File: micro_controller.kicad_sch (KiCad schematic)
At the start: 14 parts, among them J2 Conn_01x06_Male, Q7 DMN62D0U-7, U3 MCP2221A, U6 ESP32

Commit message: WIP
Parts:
- added JP3: Jumper_2_Open, Connector_PinHeader_2.54mm:PinHeader_1x02_P2.54mm_Vertical, symbol Jumper:Jumper_2_Open
- added R28: R, Resistor_SMD:R_0805_2012Metric, symbol Device:R
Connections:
- net GND: now also R7.2, R8.2, R28.2; no longer D10.1, D4.1
- net GPIO_{DATA}: now also U6.10 (IO25); no longer U6.28 (IO17)
- net GPIO_{RCLK}: now also U6.8 (IO32); no longer U6.30 (IO18)
- net GPIO_{SCLK}: now also U6.9 (IO33); no longer U6.29 (IO5)
- net SPI.CLK: now also U6.29 (IO5); no longer U6.10 (IO25)
- net SPI.MISO: now also U6.27 (IO16); no longer U6.8 (IO32)
- net SPI.MOSI: now also U6.28 (IO17); no longer U6.9 (IO33)
- net bootmode_select: now also JP3.1 (A)
- net mcu_indicator: now also D10.2, U6.33 (IO21); no longer R8.1
- net usb_indicator: now also D4.2; no longer R7.1
- net ~{GPIO_{OE}}: now also U6.12 (IO27); no longer U6.26 (IO4)
- net ~{GPIO_{RS}}: now also U6.11 (IO26); no longer U6.27 (IO16)
- net ~{INT_{CAN}}: now also U6.30 (IO18); no longer U6.12 (IO27)
- net ~{SPI.CS_{CAN}}: now also U6.26 (IO4); no longer U6.11 (IO26)
- new net: D4.1, R7.1
- new net: JP3.2 (B), R28.1
- new net: D10.1, R8.1
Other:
- note added: "Use to manually put ESP into boot mode"
- moved on the sheet: D10, D4, R7, R8

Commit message: WIP
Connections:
- net GPIO_{DATA}: now also U6.9 (IO33); no longer U6.10 (IO25)
- net GPIO_{RCLK}: now also U6.11 (IO26); no longer U6.8 (IO32)
- net GPIO_{SCLK}: now also U6.8 (IO32); no longer U6.9 (IO33)
- net ~{GPIO_{RS}}: now also U6.10 (IO25); no longer U6.11 (IO26)
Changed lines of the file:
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@@
     (effects (font (size 1.27 1.27)) (justify right))
   )
-  (hierarchical_label "GPIO_{RCLK}" (shape output) (at 148.59 96.52 180)
+  (hierarchical_label "GPIO_{SCLK}" (shape output) (at 148.59 96.52 180)
     (effects (font (size 1.27 1.27)) (justify right))
   )
-  (hierarchical_label "GPIO_{SCLK}" (shape output) (at 148.59 99.06 180)
+  (hierarchical_label "GPIO_{DATA}" (shape output) (at 148.59 99.06 180)
     (effects (font (size 1.27 1.27)) (justify right))
   )
-  (hierarchical_label "GPIO_{DATA}" (shape output) (at 148.59 101.6 180)
+  (hierarchical_label "~{GPIO_{RS}}" (shape output) (at 148.59 101.6 180)
     (effects (font (size 1.27 1.27)) (justify right))
   )
-  (hierarchical_label "~{GPIO_{RS}}" (shape output) (at 148.59 104.14 180)
+  (hierarchical_label "GPIO_{RCLK}" (shape output) (at 148.59 104.14 180)
     (effects (font (size 1.27 1.27)) (justify right))
   )

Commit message: WIP
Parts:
- removed J2: Conn_01x06_Male, Connector_PinHeader_2.54mm:PinHeader_2x03_P2.54mm_Vertical, symbol Connector:Conn_01x06_Male
- added J2: Conn_01x12_Male, Connector_PinHeader_2.54mm:PinHeader_2x06_P2.54mm_Vertical, symbol Connector:Conn_01x12_Male
- added R32, R33, R34: R, Resistor_SMD:R_0805_2012Metric, symbol Device:R
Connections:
- net GND: now also J2.6 (Pin_6), J2.9 (Pin_9)
- net SCL: now also J2.5 (Pin_5)
- net SDA: now also J2.3 (Pin_3)
- net bootmode_select: now also R34.1
- net esp_reset: now also U3.8 (GP3), R33.1
- net esp_rx: now also J2.8 (Pin_8)
- net esp_tx: now also R32.1
- net ~silent_boot: now also J2.7 (Pin_7)
- new net: J2.11 (Pin_11), R33.2
- new net: J2.10 (Pin_10), R32.2
- new net: J2.12 (Pin_12), R34.2
- new net +5V: J2.2 (Pin_2), J2.4 (Pin_4)
- no-connect marks 2 -> 3
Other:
- note added: "This header provides access to the ESP's UART, strapping pins, and I2C bus. It is designed to match the pinout of pins 1-12 of the Raspberry Pi such that a cable can connect them directly to supply data and power."
- note removed: "Debug Header"
- moved on the sheet: JP10, JP9, U3, U6

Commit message: geographical reannotate
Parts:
- renumbered C5 to C17, C6 to C2, C8 to C23, D10 to D4, D4 to D7, J2 to J1, JP3 to JP1, JP9 to JP2, JP10 to JP3, Q7 to Q1, R6 to R1, R8 to R16, R28 to R17, R34 to R18, R33 to R19, R32 to R21, R7 to R23, U6 to U1
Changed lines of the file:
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@@
   (symbol (lib_id "Jumper:SolderJumper_2_Open") (at 48.26 77.47 180) (unit 1)
     (in_bom yes) (on_board yes)
-    (property "Reference" "JP10" (id 0) (at 44.45 76.2 0)
+    (property "Reference" "JP3" (id 0) (at 44.45 76.2 0)
       (effects (font (size 1.27 1.27)) (justify left))
     )
@@
   (symbol (lib_id "Jumper:SolderJumper_2_Open") (at 48.26 80.01 180) (unit 1)
     (in_bom yes) (on_board yes)
-    (property "Reference" "JP9" (id 0) (at 43.18 78.74 0)
+    (property "Reference" "JP2" (id 0) (at 43.18 78.74 0)
       (effects (font (size 1.27 1.27)) (justify left))
     )
@@
   (symbol (lib_id "Device:R") (at 48.26 161.29 0) (unit 1)
     (in_bom yes) (on_board yes) (fields_autoplaced)
-    (property "Reference" "R6" (id 0) (at 50.8 160.0199 0)
+    (property "Reference" "R1" (id 0) (at 50.8 160.0199 0)
       (effects (font (size 1.27 1.27)) (justify left))
     )
@@
   (symbol (lib_id "Device:R") (at 76.2 181.61 0) (unit 1)
     (in_bom yes) (on_board yes) (fields_autoplaced)
-    (property "Reference" "R7" (id 0) (at 78.74 180.3399 0)
+    (property "Reference" "R23" (id 0) (at 78.74 180.3399 0)
       (effects (font (size 1.27 1.27)) (justify left))
     )
@@
   (symbol (lib_id "Device:R") (at 86.36 181.61 0) (unit 1)
     (in_bom yes) (on_board yes) (fields_autoplaced)
-    (property "Reference" "R8" (id 0) (at 88.9 180.3399 0)
+    (property "Reference" "R16" (id 0) (at 88.9 180.3399 0)
       (effects (font (size 1.27 1.27)) (justify left))
     )
@@
   (symbol (lib_id "Device:R") (at 147.32 180.34 0) (unit 1)
     (in_bom yes) (on_board yes) (fields_autoplaced)
-    (property "Reference" "R28" (id 0) (at 149.86 179.0699 0)
+    (property "Reference" "R17" (id 0) (at 149.86 179.0699 0)
       (effects (font (size 1.27 1.27)) (justify left))
     )
@@
   (symbol (lib_id "Device:R") (at 250.19 48.26 90) (unit 1)
     (in_bom yes) (on_board yes)
-    (property "Reference" "R32" (id 0) (at 255.27 46.99 90))
+    (property "Reference" "R21" (id 0) (at 255.27 46.99 90))
     (property "Value" "R" (id 1) (at 250.19 48.26 90))
     (property "Footprint" "Resistor_SMD:R_0805_2012Metric" (id 2) (at 250.19 50.038 90)
@@
   (symbol (lib_id "Device:R") (at 250.19 50.8 90) (unit 1)
     (in_bom yes) (on_board yes)
-    (property "Reference" "R33" (id 0) (at 255.27 49.53 90))
+    (property "Reference" "R19" (id 0) (at 255.27 49.53 90))
     (property "Value" "R" (id 1) (at 250.19 50.8 90))
     (property "Footprint" "Resistor_SMD:R_0805_2012Metric" (id 2) (at 250.19 52.578 90)
@@
   (symbol (lib_id "Device:R") (at 250.19 53.34 90) (unit 1)
     (in_bom yes) (on_board yes)
-    (property "Reference" "R34" (id 0) (at 255.27 52.07 90))
+    (property "Reference" "R18" (id 0) (at 255.27 52.07 90))
     (property "Value" "R" (id 1) (at 250.19 53.34 90))
     (property "Footprint" "Resistor_SMD:R_0805_2012Metric" (id 2) (at 250.19 55.118 90)
@@
   (symbol (lib_id "Jumper:Jumper_2_Open") (at 147.32 171.45 270) (unit 1)
     (in_bom yes) (on_board yes)
-    (property "Reference" "JP3" (id 0) (at 149.86 170.1799 90)
+    (property "Reference" "JP1" (id 0) (at 149.86 170.1799 90)
       (effects (font (size 1.27 1.27)) (justify left))
     )
@@
   (symbol (lib_id "ecafe-racer:LED_Green") (at 76.2 173.99 90) (unit 1)
     (in_bom yes) (on_board yes) (fields_autoplaced)
-    (property "Reference" "D4" (id 0) (at 80.01 172.9104 90)
+    (property "Reference" "D7" (id 0) (at 80.01 172.9104 90)
       (effects (font (size 1.27 1.27)) (justify right))
     )
@@
   (symbol (lib_id "ecafe-racer:LED_Green") (at 86.36 173.99 90) (unit 1)
     (in_bom yes) (on_board yes) (fields_autoplaced)
-    (property "Reference" "D10" (id 0) (at 90.17 172.9104 90)
+    (property "Reference" "D4" (id 0) (at 90.17 172.9104 90)
       (effects (font (size 1.27 1.27)) (justify right))
     )
@@
   (symbol (lib_id "Device:C") (at 48.26 175.26 0) (unit 1)
     (in_bom yes) (on_board yes) (fields_autoplaced)
-    (property "Reference" "C5" (id 0) (at 52.07 173.9899 0)
+    (property "Reference" "C17" (id 0) (at 52.07 173.9899 0)
       (effects (font (size 1.27 1.27)) (justify left))
     )
@@
   (symbol (lib_id "Device:C") (at 204.47 152.4 0) (unit 1)
     (in_bom yes) (on_board yes) (fields_autoplaced)
-    (property "Reference" "C6" (id 0) (at 208.28 151.1299 0)
+    (property "Reference" "C2" (id 0) (at 208.28 151.1299 0)
       (effects (font (size 1.27 1.27)) (justify left))
     )
@@
   (symbol (lib_id "Device:C") (at 217.17 152.4 0) (unit 1)
     (in_bom yes) (on_board yes) (fields_autoplaced)
-    (property "Reference" "C8" (id 0) (at 220.98 151.1299 0)
+    (property "Reference" "C23" (id 0) (at 220.98 151.1299 0)
       (effects (font (size 1.27 1.27)) (justify left))
     )
@@
   (symbol (lib_id "ecafe-racer:DMN62D0U-7") (at 39.37 175.26 0) (unit 1)
     (in_bom yes) (on_board yes)
-    (property "Reference" "Q7" (id 0) (at 31.75 170.1799 0)
+    (property "Reference" "Q1" (id 0) (at 31.75 170.1799 0)
       (effects (font (size 1.27 1.27)) (justify left))
     )
@@
   (symbol (lib_id "Connector:Conn_01x12_Male") (at 265.43 38.1 0) (mirror y) (unit 1)
     (in_bom yes) (on_board yes)
-    (property "Reference" "J2" (id 0) (at 267.97 38.0999 0)
+    (property "Reference" "J1" (id 0) (at 267.97 38.0999 0)
       (effects (font (size 1.27 1.27)) (justify right))
     )
@@
   (symbol (lib_id "ecafe-racer:ESP32") (at 156.21 74.93 0) (unit 1)
     (in_bom yes) (on_board yes) (fields_autoplaced)
-    (property "Reference" "U6" (id 0) (at 155.575 46.99 0))
+    (property "Reference" "U1" (id 0) (at 155.575 46.99 0))
     (property "Value" "ESP32" (id 1) (at 155.575 49.53 0))
     (property "Footprint" "ecafe-racer:MODULE_ESP32-WROOM-32" (id 2) (at 149.606 50.038 0)

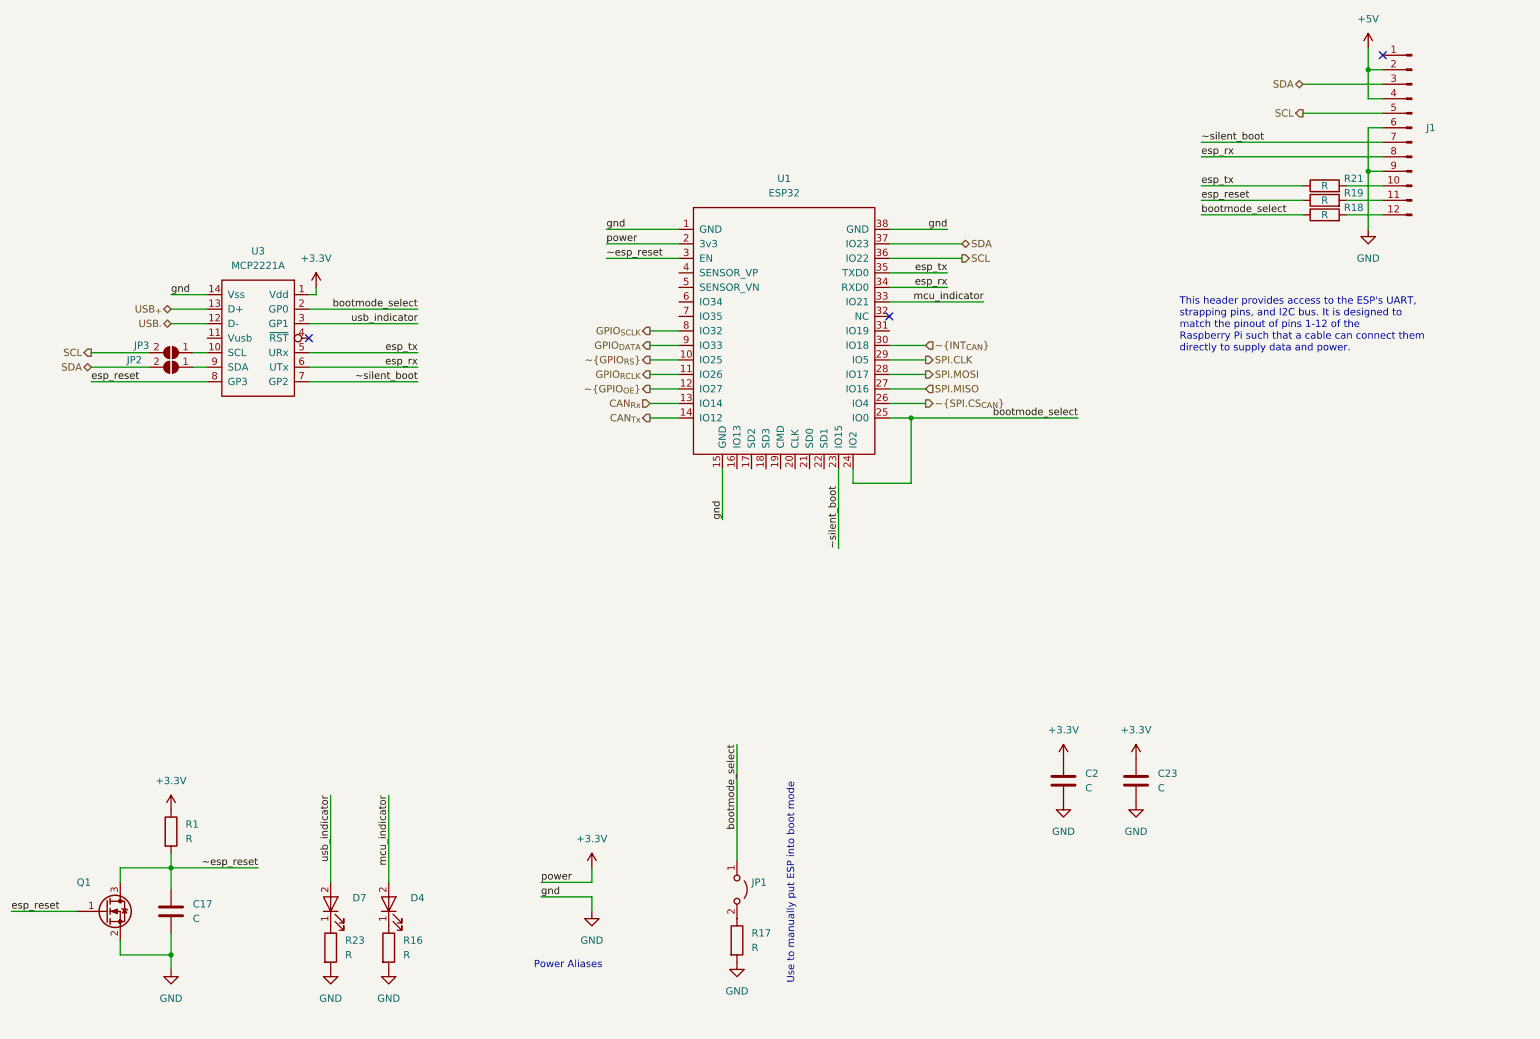
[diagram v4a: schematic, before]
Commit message: cleaned up schematic
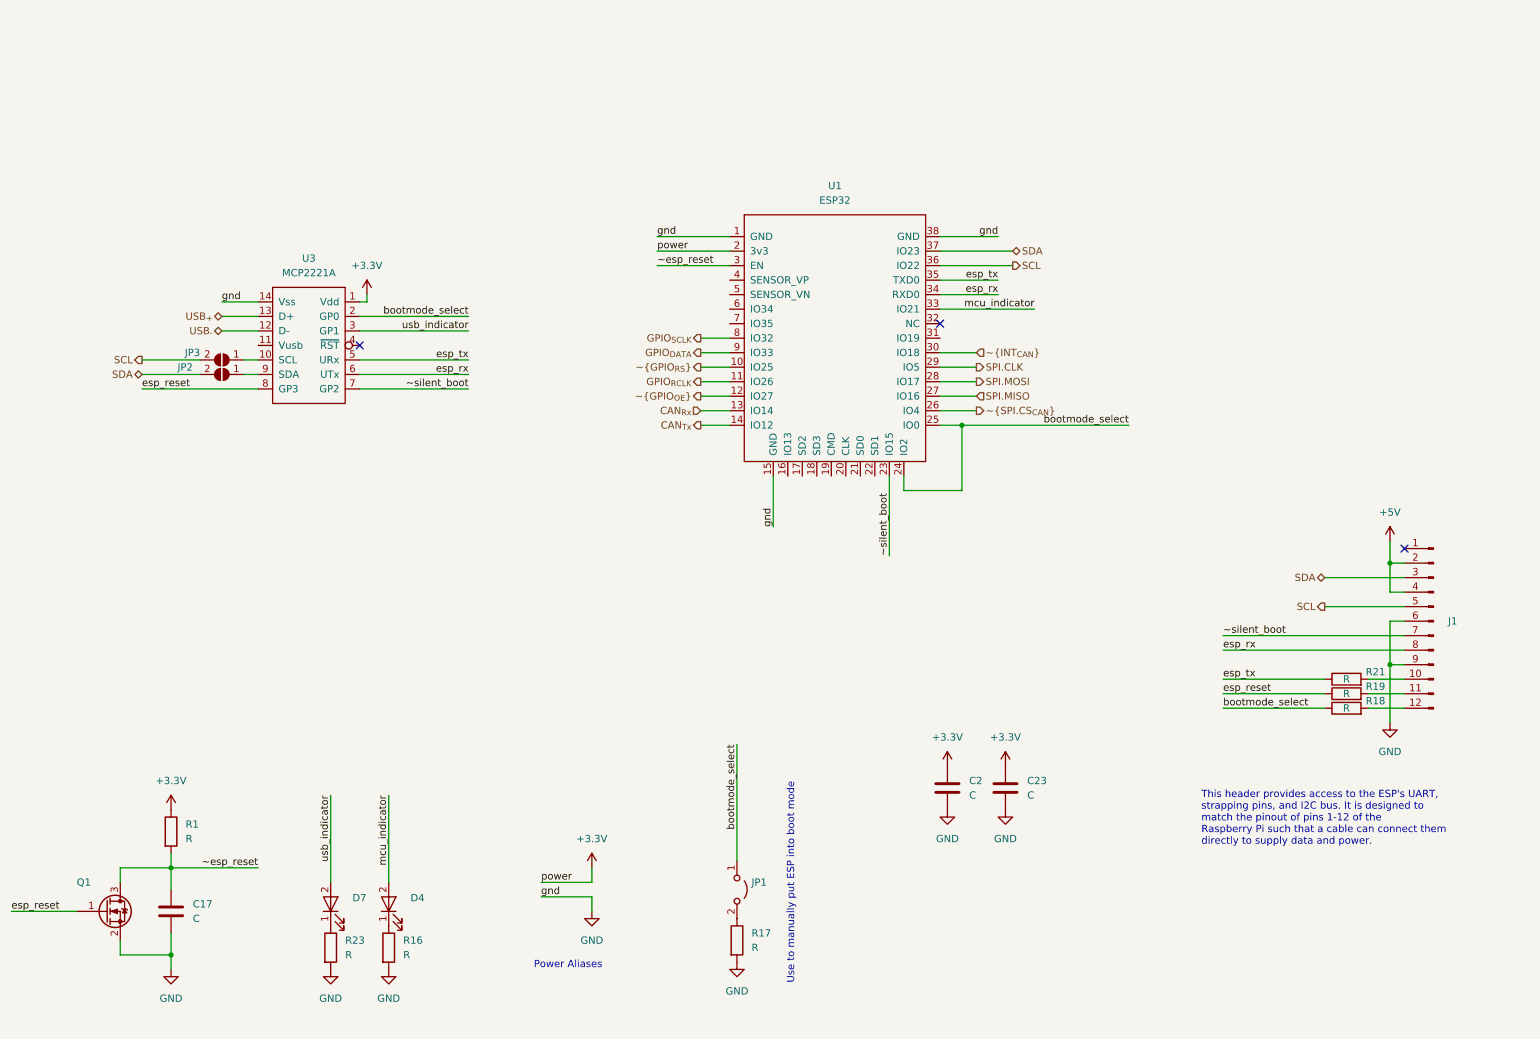
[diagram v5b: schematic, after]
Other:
- moved on the sheet: C2, C23, J1, JP2, JP3, R18, R19, R21, U1, U3

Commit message: Forgot to connect the interrupt signal for the GPIO
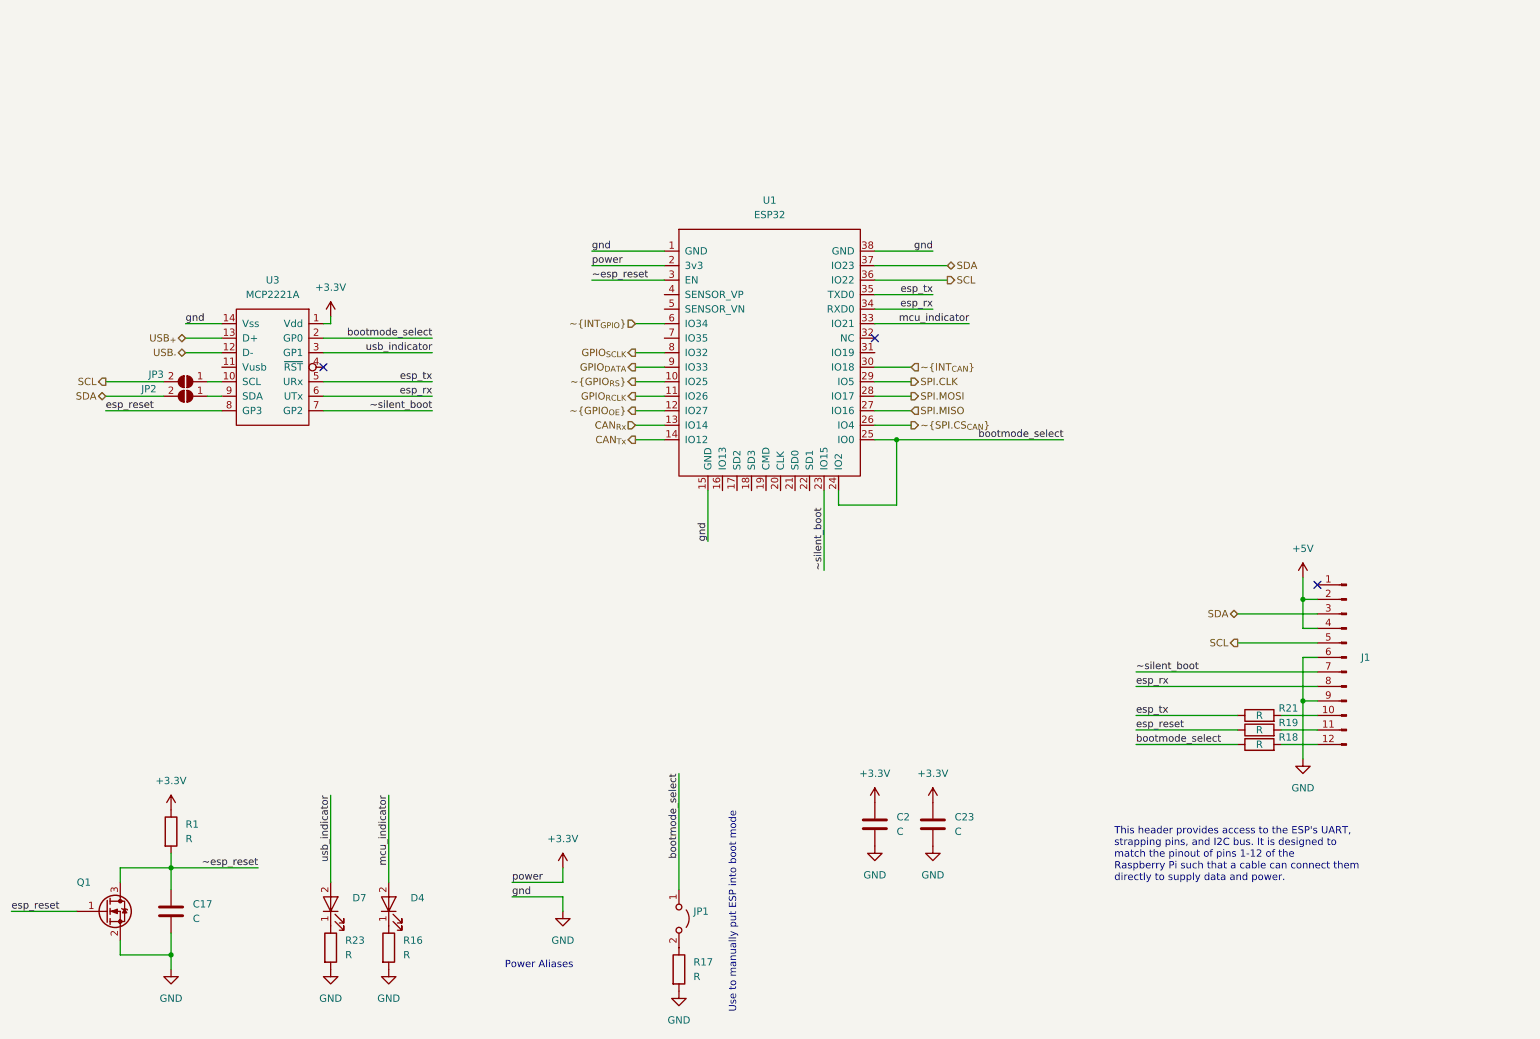
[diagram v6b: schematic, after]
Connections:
- net ~{INT_{GPIO}}: now reaches U1.6 (IO34)
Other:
- moved on the sheet: C2, C23, J1, JP1, JP2, JP3, R17, R18, R19, R21, U1, U3
